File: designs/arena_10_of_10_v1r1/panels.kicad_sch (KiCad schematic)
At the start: 0 parts

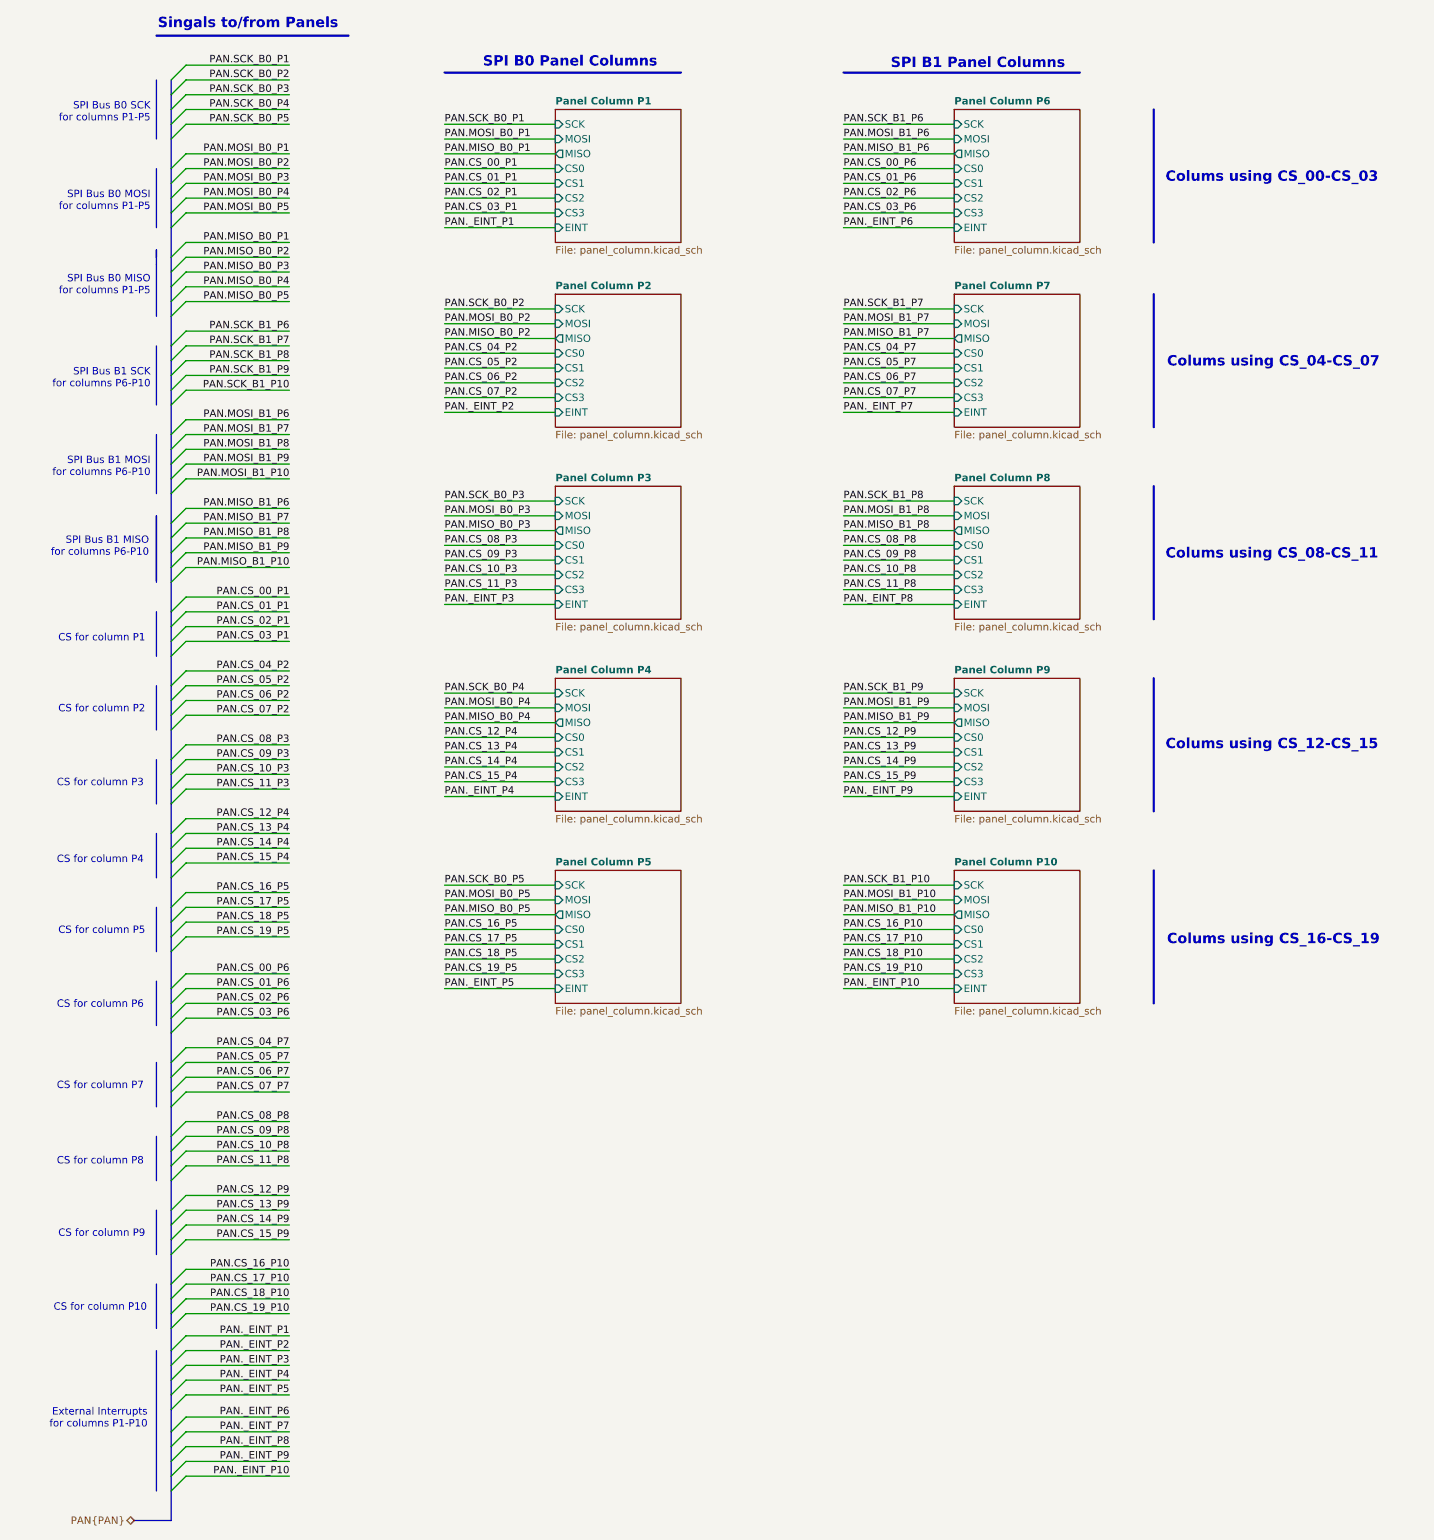
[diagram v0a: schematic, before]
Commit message: Working through schematic design rule check.
Just some power issues remaing.
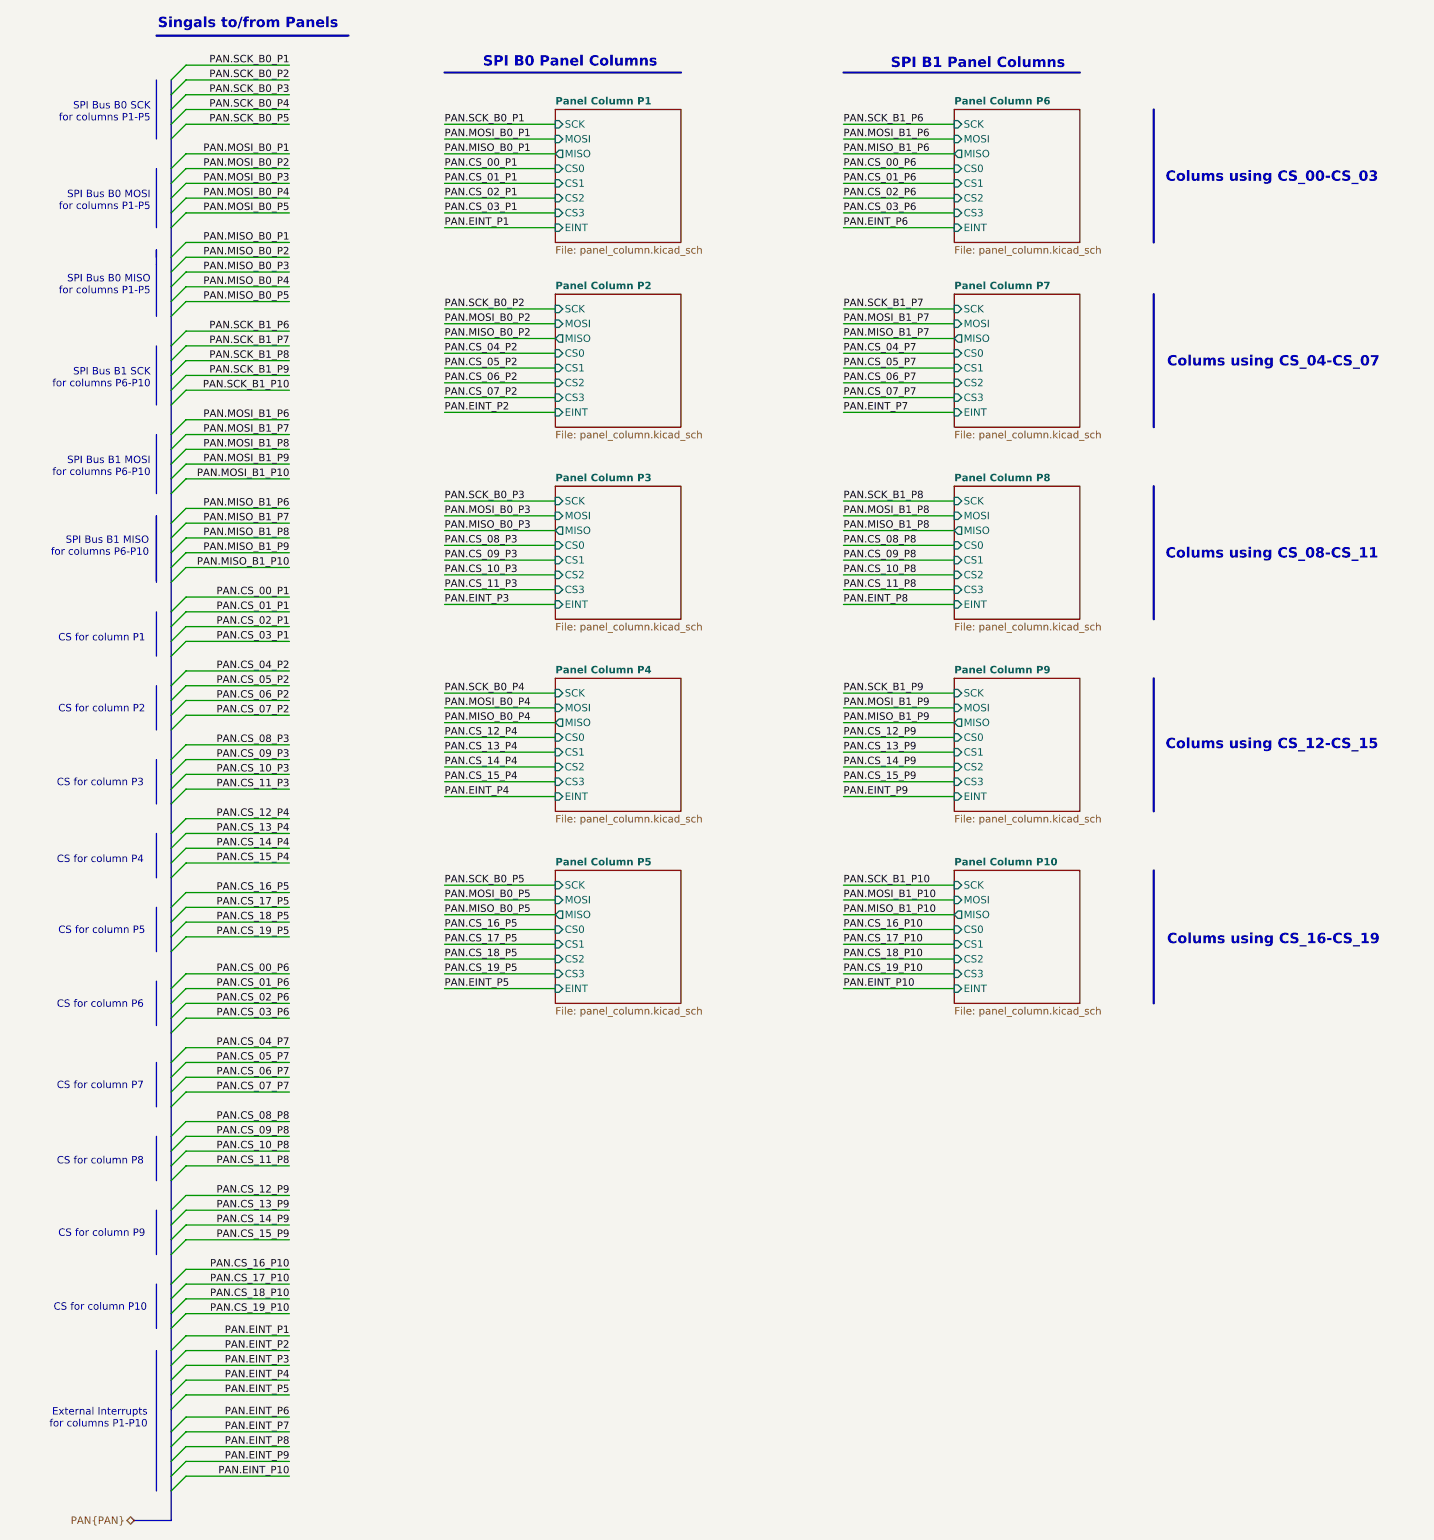
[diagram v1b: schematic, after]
